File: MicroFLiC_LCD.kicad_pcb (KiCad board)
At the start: 2 copper layers, 50 x 50 mm, 21 parts, among them P1 2x8 header strip, Q1 BCX54-16, U1 MCP4728, U2 TLV2371, U3 74AHCT367, U4 74AHCT367

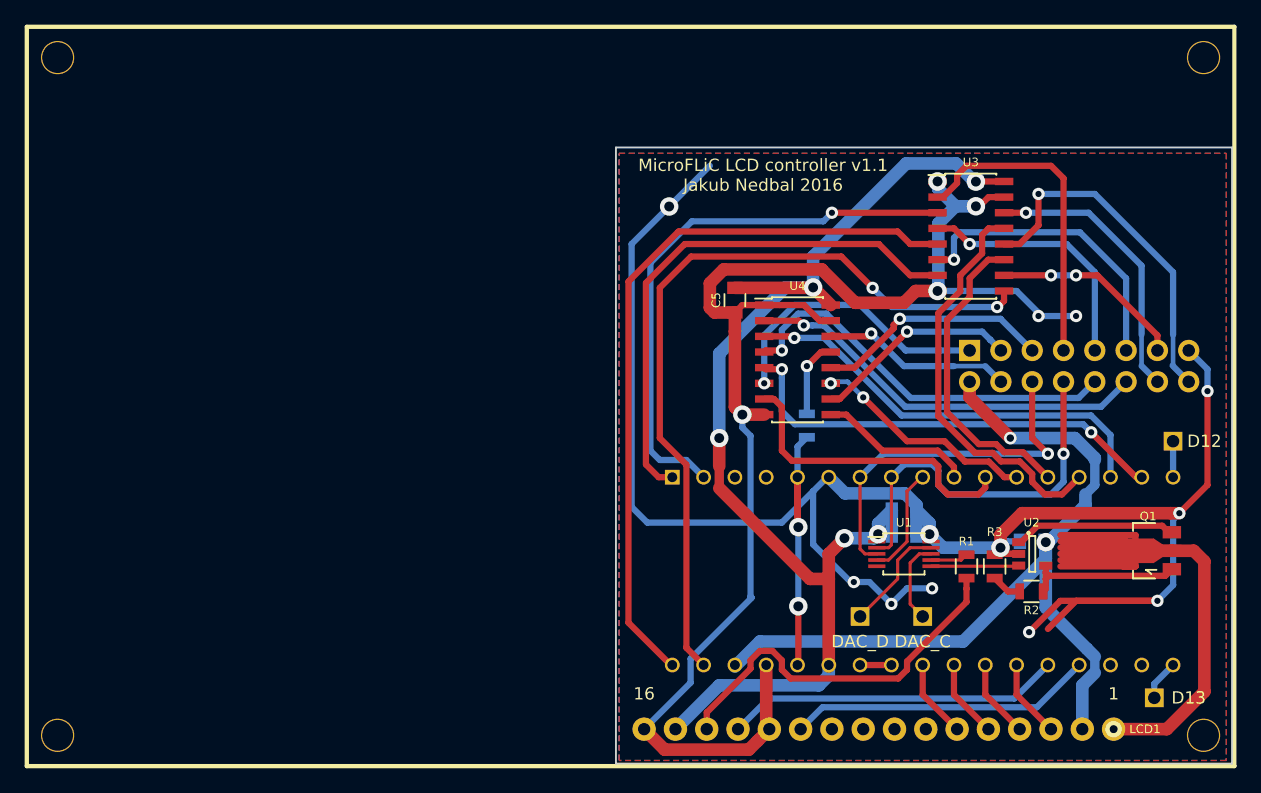
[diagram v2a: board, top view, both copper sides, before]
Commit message: Fixed LCD orientation, added powerful emitter-follower amplifier
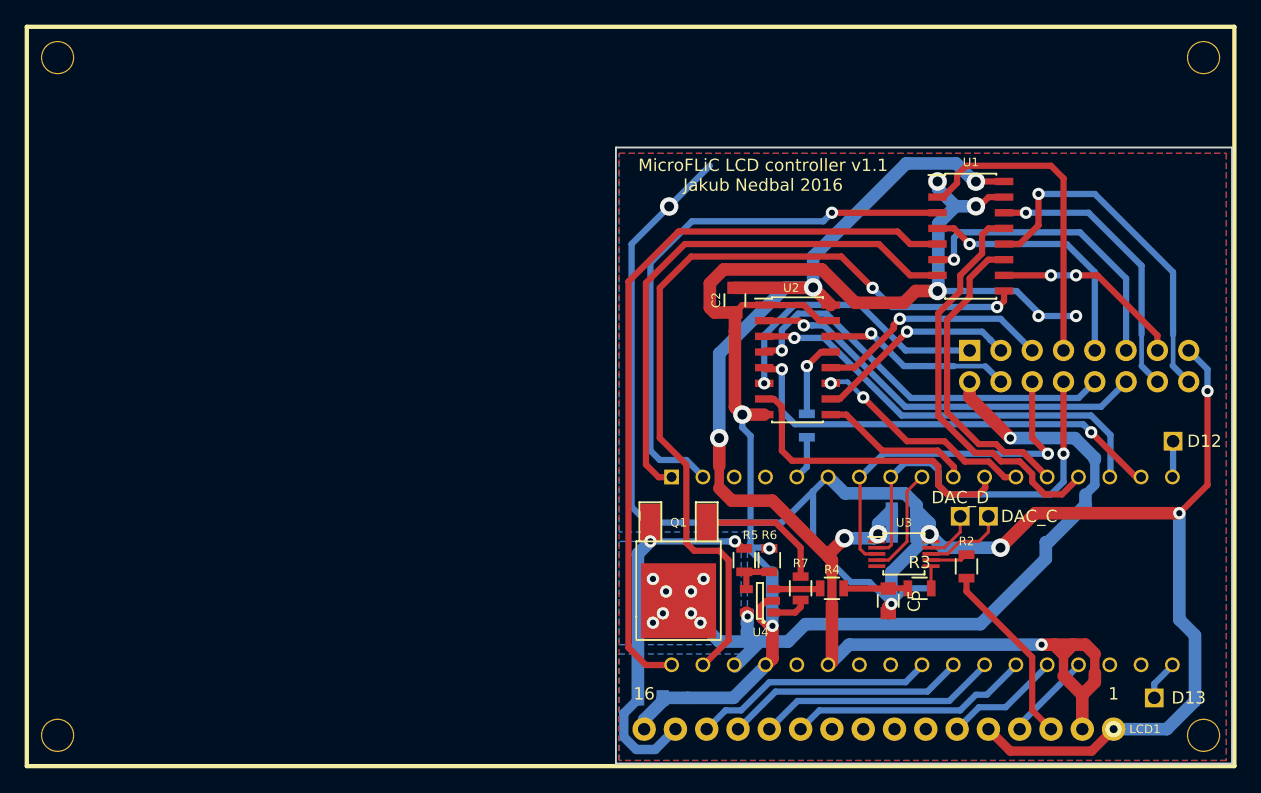
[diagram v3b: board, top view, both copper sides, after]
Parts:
- removed the R2 at (116.0, 146.3)
- added C5: 4u7/25V, Capacitors_SMD:C_0805, F.Cu at (104.4, 147.1)
- added C7: 4u7/25V, Capacitors_SMD:C_0805, B.Cu at (85.1, 154.9)
- added R1: 1k5, Resistors_SMD:R_0805, B.Cu at (97.8, 132.8)
- added R5: 10k, Resistors_SMD:R_0805, F.Cu at (94.7, 143.8)
- added R6: 10k, Resistors_SMD:R_0805, F.Cu at (92.7, 143.8)
- added R7: 47R, Resistors_SMD:R_0805, F.Cu at (97.3, 146.1)
- C3: renamed from C1; value 10u/10V -> 4u7/25V
- Q1: value BCX54-16 -> MJD31CT4G; footprint TO_SOT_Packages_SMD:SOT89-3_Housing -> TO_SOT_Packages_SMD:TO-252-2Lead
- R3: value 18R(0.5W) -> 100k
- R4: value 1k5 -> 10k; moved to F.Cu
- moved Q1 38.3 mm to (87.4, 140.7), turned to 180 degrees
- moved C6 22.9 mm to (94.0, 148.3), turned to 0 degrees
- moved U4 22.4 mm to (94.0, 147.1), turned to 180 degrees
- moved PP4 21.6 mm to (110.2, 140.2)
- moved PP2 19.9 mm to (126.0, 154.9)
- moved R4 13.4 mm to (99.8, 146.1), turned to 0 degrees
- moved PP3 13.2 mm to (112.5, 140.2)
- moved R3 6.35 mm to (106.9, 146.1), turned to 0 degrees
- moved A1 0.06 mm to (83.3, 135.6)
- renumbered C4 to C1, C5 to C2, C2 to C4, C3 to C6, R1 to R2, U3 to U1, U4 to U2, U1 to U3, U2 to U4
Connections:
- net /SCL renamed /DAC/SCL
- net /SDA renamed /DAC/SDA
- net /~LDAC renamed /DAC/~LDAC
- A1 pad A0: /LCD_E -> /LCD_RS
- A1 pad A1: /LCD_RS -> /LCD_E
- A1 pad A2: /LCD_D7 -> /LCD_D4
- A1 pad A3: /LCD_D6 -> /LCD_D5
- A1 pad A4: /LCD_D5 -> /LCD_D6
- A1 pad A5: /LCD_D4 -> /LCD_D7
- LCD1 pad 1: /LCD_BKL -> GND
- LCD1 pad 11: /LCD_E -> /LCD_D4
- LCD1 pad 12: GND -> /LCD_D5
- LCD1 pad 13: /LCD_RS -> /LCD_D6
- LCD1 pad 14: /LCD_CONT -> /LCD_D7
- LCD1 pad 15: +5V -> /DAC/LCD_BKL
- LCD1 pad 2: +12V -> +5V
- LCD1 pad 3: /LCD_D7 -> /DAC/LCD_CONT
- LCD1 pad 4: /LCD_D6 -> /LCD_RS
- LCD1 pad 5: /LCD_D5 -> GND
- LCD1 pad 6: /LCD_D4 -> /LCD_E
- PP2 pad 1: /DAC_C -> /D13
- PP3 pad 1: /DAC_D -> /DAC/DAC_C
- PP4 pad 1: /D13 -> /DAC/DAC_D
- Q1 pad 2: /LCD_BKL -> +12V
- Q1 pad 3: Net-(Q1-Pad3) -> /DAC/LCD_BKL
- R2 pad 1: /LCD_CONT -> /DAC/LCD_CONT
- R3 pad 1: Net-(R2-Pad2) (its old number) -> Net-(C5-Pad1)
- R3 pad 2: GND -> /DAC/LCD_BKL_CTRL
- R4 pad 1: /3V3to5V/~RST_5V -> Net-(R4-Pad1)
- R4 pad 2: Net-(R4-Pad2) -> Net-(C5-Pad1)
- U2 pad 13: Net-(R4-Pad2) -> Net-(R1-Pad2)
- U3 pad 6: /LCD_BKL_CTRL -> /DAC/LCD_BKL_CTRL
- U3 pad 8: /DAC_C -> /DAC/DAC_C
- U3 pad 9: /DAC_D -> /DAC/DAC_D
- U4 pad 1: Net-(Q1-Pad3) -> Net-(R7-Pad2)
- U4 pad 3: /LCD_BKL_CTRL -> Net-(R4-Pad1)
- U4 pad 4: Net-(Q1-Pad1) -> Net-(R5-Pad1)
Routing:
- net /LCD_BKL: track 64.0 -> 0.00 mm
- net /DAC/LCD_BKL: track 0.00 -> 31.4 mm, vias 0 -> 2
- net /LCD_CONT: track 31.2 -> 0.00 mm
- net /LCD_RS: track 27.3 -> 7.20 mm
- net +5V: track 97.9 -> 117.3 mm, vias 5 -> 6
- net /3V3to5V/~RST_5V: track 22.9 -> 3.56 mm, vias 2 -> 0
- net +12V: track 69.5 -> 86.4 mm, vias 2 -> 10
- net /LCD_E: track 24.8 -> 9.52 mm
- net /DAC/LCD_CONT: track 0.00 -> 15.1 mm
- net /LCD_D5: track 6.36 -> 20.0 mm
- net /LCD_D4: track 6.36 -> 19.7 mm
- net /LCD_D7: track 6.36 -> 19.7 mm
- net /LCD_D6: track 6.36 -> 19.7 mm
- net Net-(Q1-Pad3): track 13.2 -> 0.00 mm
- net /DAC_D: track 8.96 -> 0.00 mm
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- added copper zone on B.Cu, net +12V

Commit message: Finalized PCB for production
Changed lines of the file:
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@@
-    )
-  )
-  (module jakub:LCD2004 (layer F.Cu)
-    (at 83.482 130.48)
-    (fp_text reference LCD1 (at 41.74 27) (layer F.SilkS)
-      (effects (font (size 0.7 0.7) (thickness 0.11)))
-    )
-    (fp_text value LCD2004 (at 0 1.27) (layer F.Fab) hide
-      (effects (font (size 1 1) (thickness 0.15)))
-    )
-    (fp_text user 1 (at 39.2 24.13) (layer F.SilkS)
-      (effects (font (size 1 1) (thickness 0.15)))
-    )
-    (fp_text user 16 (at 1.1 24.13) (layer F.SilkS)
-      (effects (font (size 1 1) (thickness 0.15)))
-    )
-    (fp_circle (center 39.2 27) (end 39.7 27) (layer F.SilkS) (width 0.35))
-    (fp_line (start -49 -30) (end 49 -30) (layer F.SilkS) (width 0.35))
-    (fp_line (start 49 30) (end 49 -30) (layer F.SilkS) (width 0.35))
-    (fp_line (start -49 30) (end 49 30) (layer F.SilkS) (width 0.35))
-    (fp_line (start -49 -30) (end -49 30) (layer F.SilkS) (width 0.35))
-    (pad 1 thru_hole circle (at 39.2 27) (size 1.9 1.9) (drill 1) (layers *.Cu *.Mask F.SilkS)
-      (net 2 GND))
-    (pad 2 thru_hole circle (at 36.66 27) (size 1.9 1.9) (drill 1) (layers *.Cu *.Mask F.SilkS)
-      (net 3 +5V))
-    (pad 3 thru_hole circle (at 34.12 27) (size 1.9 1.9) (drill 1) (layers *.Cu *.Mask F.SilkS)
-      (net 44 /DAC/LCD_CONT))
-    (pad 4 thru_hole circle (at 31.58 27) (size 1.9 1.9) (drill 1) (layers *.Cu *.Mask F.SilkS)
-      (net 9 /LCD_RS))
-    (pad 5 thru_hole circle (at 29.04 27) (size 1.9 1.9) (drill 1) (layers *.Cu *.Mask F.SilkS)
-      (net 2 GND))
-    (pad 6 thru_hole circle (at 26.5 27) (size 1.9 1.9) (drill 1) (layers *.Cu *.Mask F.SilkS)
-      (net 8 /LCD_E))
-    (pad 7 thru_hole circle (at 23.96 27) (size 1.9 1.9) (drill 1) (layers *.Cu *.Mask F.SilkS))
-    (pad 8 thru_hole circle (at 21.42 27) (size 1.9 1.9) (drill 1) (layers *.Cu *.Mask F.SilkS))
-    (pad 9 thru_hole circle (at 18.88 27) (size 1.9 1.9) (drill 1) (layers *.Cu *.Mask F.SilkS))
-    (pad 10 thru_hole circle (at 16.34 27) (size 1.9 1.9) (drill 1) (layers *.Cu *.Mask F.SilkS))
-    (pad 11 thru_hole circle (at 13.8 27) (size 1.9 1.9) (drill 1) (layers *.Cu *.Mask F.SilkS)
-      (net 7 /LCD_D4))
-    (pad 12 thru_hole circle (at 11.26 27) (size 1.9 1.9) (drill 1) (layers *.Cu *.Mask F.SilkS)
-      (net 6 /LCD_D5))
-    (pad 13 thru_hole circle (at 8.72 27) (size 1.9 1.9) (drill 1) (layers *.Cu *.Mask F.SilkS)
-      (net 5 /LCD_D6))
-    (pad 14 thru_hole circle (at 6.18 27) (size 1.9 1.9) (drill 1) (layers *.Cu *.Mask F.SilkS)
-      (net 4 /LCD_D7))
-    (pad 15 thru_hole circle (at 3.64 27) (size 1.9 1.9) (drill 1) (layers *.Cu *.Mask F.SilkS)
-      (net 43 /DAC/LCD_BKL))
-    (pad 16 thru_hole circle (at 1.1 27) (size 1.9 1.9) (drill 1) (layers *.Cu *.Mask F.SilkS)
-      (net 2 GND))
-    (pad "" np_thru_hole circle (at -46.5 -27.5) (size 2.7 2.7) (drill 2.5) (layers *.Cu *.Mask F.SilkS))
-    (pad "" np_thru_hole circle (at 46.5 -27.5) (size 2.7 2.7) (drill 2.5) (layers *.Cu *.Mask F.SilkS))
-    (pad "" np_thru_hole circle (at 46.5 27.5) (size 2.7 2.7) (drill 2.5) (layers *.Cu *.Mask F.SilkS))
-    (pad "" np_thru_hole circle (at -46.5 27.5) (size 2.7 2.7) (drill 2.5) (layers *.Cu *.Mask F.SilkS))
-    (model jakub.3dshapes/displays/lcd2004.wrl
-      (at (xyz 0 0 0.45))
-      (scale (xyz 0.3937 0.3937 0.3937))
-      (rotate (xyz 0 0 0))
-    )
-    (model Pin_Headers.3dshapes/Pin_Header_Straight_1x16.wrl
-      (at (xyz 0.794 -1.066929 0.4475))
-      (scale (xyz 1 1 1))
-      (rotate (xyz 0 180 0))
-    )
-    (model Socket_Strips.3dshapes/Socket_Strip_Straight_1x16.wrl
-      (at (xyz 0.794 -1.066929 0))
-      (scale (xyz 1 1 1))
-      (rotate (xyz 0 0 0))
     )
   )
@@
     )
   )
+  (module jakub:LCD2004 (layer F.Cu)
+    (at 83.482 130.48)
+    (fp_text reference LCD1 (at 41.74 27) (layer F.SilkS)
+      (effects (font (size 0.7 0.7) (thickness 0.11)))
+    )
+    (fp_text value LCD2004 (at 0 1.27) (layer F.Fab) hide
+      (effects (font (size 1 1) (thickness 0.15)))
+    )
+    (fp_circle (center 46.5 -27.5) (end 46.5 -28.5) (layer F.SilkS) (width 0.35))
+    (fp_circle (center -46.5 -27.5) (end -46.5 -28.5) (layer F.SilkS) (width 0.35))
+    (fp_circle (center -46.5 27.5) (end -46.5 28.5) (layer F.SilkS) (width 0.35))
+    (fp_text user 1 (at 39.2 24.13) (layer F.SilkS)
+      (effects (font (size 1 1) (thickness 0.15)))
+    )
+    (fp_text user 16 (at 1.1 24.13) (layer F.SilkS)
+      (effects (font (size 1 1) (thickness 0.15)))
+    )
+    (fp_circle (center 39.2 27) (end 39.7 27) (layer F.SilkS) (width 0.35))
+    (fp_line (start -49 -30) (end 49 -30) (layer F.SilkS) (width 0.35))
+    (fp_line (start 49 30) (end 49 -30) (layer F.SilkS) (width 0.35))
+    (fp_line (start -49 30) (end 49 30) (layer F.SilkS) (width 0.35))
+    (fp_line (start -49 -30) (end -49 30) (layer F.SilkS) (width 0.35))
+    (pad 1 thru_hole circle (at 39.2 27) (size 1.9 1.9) (drill 1) (layers *.Cu *.Mask F.SilkS)
+      (net 2 GND))
+    (pad 2 thru_hole circle (at 36.66 27) (size 1.9 1.9) (drill 1) (layers *.Cu *.Mask F.SilkS)
+      (net 3 +5V))
+    (pad 3 thru_hole circle (at 34.12 27) (size 1.9 1.9) (drill 1) (layers *.Cu *.Mask F.SilkS)
+      (net 44 /DAC/LCD_CONT))
+    (pad 4 thru_hole circle (at 31.58 27) (size 1.9 1.9) (drill 1) (layers *.Cu *.Mask F.SilkS)
+      (net 9 /LCD_RS))
+    (pad 5 thru_hole circle (at 29.04 27) (size 1.9 1.9) (drill 1) (layers *.Cu *.Mask F.SilkS)
+      (net 2 GND))
+    (pad 6 thru_hole circle (at 26.5 27) (size 1.9 1.9) (drill 1) (layers *.Cu *.Mask F.SilkS)
+      (net 8 /LCD_E))
+    (pad 7 thru_hole circle (at 23.96 27) (size 1.9 1.9) (drill 1) (layers *.Cu *.Mask F.SilkS))
+    (pad 8 thru_hole circle (at 21.42 27) (size 1.9 1.9) (drill 1) (layers *.Cu *.Mask F.SilkS))
+    (pad 9 thru_hole circle (at 18.88 27) (size 1.9 1.9) (drill 1) (layers *.Cu *.Mask F.SilkS))
+    (pad 10 thru_hole circle (at 16.34 27) (size 1.9 1.9) (drill 1) (layers *.Cu *.Mask F.SilkS))
+    (pad 11 thru_hole circle (at 13.8 27) (size 1.9 1.9) (drill 1) (layers *.Cu *.Mask F.SilkS)
+      (net 7 /LCD_D4))
+    (pad 12 thru_hole circle (at 11.26 27) (size 1.9 1.9) (drill 1) (layers *.Cu *.Mask F.SilkS)
+      (net 6 /LCD_D5))
+    (pad 13 thru_hole circle (at 8.72 27) (size 1.9 1.9) (drill 1) (layers *.Cu *.Mask F.SilkS)
+      (net 5 /LCD_D6))
+    (pad 14 thru_hole circle (at 6.18 27) (size 1.9 1.9) (drill 1) (layers *.Cu *.Mask F.SilkS)
+      (net 4 /LCD_D7))
+    (pad 15 thru_hole circle (at 3.64 27) (size 1.9 1.9) (drill 1) (layers *.Cu *.Mask F.SilkS)
+      (net 43 /DAC/LCD_BKL))
+    (pad 16 thru_hole circle (at 1.1 27) (size 1.9 1.9) (drill 1) (layers *.Cu *.Mask F.SilkS)
+      (net 2 GND))
+    (pad "" np_thru_hole circle (at 46.5 27.5) (size 2.7 2.7) (drill 2.5) (layers *.Cu *.Mask F.SilkS))
+    (model jakub.3dshapes/displays/lcd2004.wrl
+      (at (xyz 0 0 0.45))
+      (scale (xyz 0.3937 0.3937 0.3937))
+      (rotate (xyz 0 0 0))
+    )
+    (model Pin_Headers.3dshapes/Pin_Header_Straight_1x16.wrl
+      (at (xyz 0.794 -1.066929 0.4475))
+      (scale (xyz 1 1 1))
+      (rotate (xyz 0 180 0))
+    )
+    (model Socket_Strips.3dshapes/Socket_Strip_Straight_1x16.wrl
+      (at (xyz 0.794 -1.066929 0))
+      (scale (xyz 1 1 1))
+      (rotate (xyz 0 0 0))
+    )
+  )
